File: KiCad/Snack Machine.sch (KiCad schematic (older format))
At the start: 149 parts, among them J1 MDB, J10 Row Screw Terminal, J11 Column Screw Terminal, J12 Display Serial Header, J13 RFID_CONNECTOR, J14 Large Display Header, J2 Power Screw Terminal, J3 RFID Serial Connector, J4 RFID Led Connector, J5 MDB, J6 Door Switch Terminal, J7 LCD EXP1, J8 LCD EXP2, J9 AVR-ISP-6, Q1 P-CH 30V 3.8A, SW1 SW_SPST, U1 MEZD71201A-F, U2 MEZD71202A-G, U3 ATmega2560-16AU, Y1 16MHz

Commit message: Fixing small issue with a missing $EndComp
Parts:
- added D7: D_Schottky, Diodes_SMD:D_SOD-323, symbol Device:D_Schottky
- TP65: Manufacturer Toshiba Semiconductor and Storage -> (none); Part Number CUS10S40,H3F -> (none)
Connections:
- wire segments 386 -> 387
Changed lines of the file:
@@
 	1    4700 1250
 	-1   0    0    1
+$EndComp
 Text Label 13700 7850 2    50   ~ 0
 TX_DISPLAY

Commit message: removed D1 and D3, left Schottky diodes alone
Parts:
- removed D1: D_Zener, Diode_SMD:D_SMB_Handsoldering, symbol Device:D_Zener
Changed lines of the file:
@@
 	4550 1250 4100 1250
-$Comp
-L Device:D_Zener D?
-U 1 1 5BF22396
-P 4700 1250
-AR Path="/5BCD883C/5BF22396" Ref="D?"  Part="1"
-AR Path="/5BF22396" Ref="D1"  Part="1"
-F 0 "D1" H 4700 1034 50  0000 C CNN
-F 1 "D_Zener" H 4700 1125 50  0000 C CNN
-F 2 "Diode_SMD:D_SMB_Handsoldering" H 4700 1250 50  0001 C CNN
-F 3 "~" H 4700 1250 50  0001 C CNN
-F 4 "Micro Commercial" H 4700 1250 50  0001 C CNN "Manufacturer"
-F 5 "3SMBJ5925B-TP" H 4700 1250 50  0001 C CNN "Part Number"
-	1    4700 1250
-	-1   0    0    1
-$EndComp
 $Comp
 L power:+5V #PWR?

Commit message: tweaked ethernet
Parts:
- D7: footprint Diodes_SMD:D_SOD-323 -> Diode_SMD:D_SOD-323
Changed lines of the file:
@@
 F 0 "D7" H 4700 1034 50  0000 C CNN
 F 1 "D_Schottky" H 4700 1125 50  0000 C CNN
-F 2 "Diodes_SMD:D_SOD-323" H 4700 1250 50  0001 C CNN
+F 2 "Diode_SMD:D_SOD-323" H 4700 1250 50  0001 C CNN
 F 3 "~" H 4700 1250 50  0001 C CNN
 F 4 "Toshiba Semiconductor and Storage" H 4700 1250 50  0001 C CNN "Manufacturer"

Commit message: added footprints for Y3 FB1 FB3 FB2 F1
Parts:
- F1: footprint (none) -> Snack Machine:Keystone_3544-2
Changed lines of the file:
@@
 F 0 "F1" V 1853 1250 50  0000 C CNN
 F 1 "1A" V 1944 1250 50  0000 C CNN
-F 2 "" V 1980 1250 50  0001 C CNN
+F 2 "Snack Machine:Keystone_3544-2" V 1980 1250 50  0001 C CNN
 F 3 "~" H 2050 1250 50  0001 C CNN
 F 4 "Keystone Electronics" V 2050 1250 50  0001 C CNN "Manufacturer"

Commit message: updated motor drive circuitry, annotated
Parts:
- removed J6: Door Switch Terminal, TerminalBlock_Phoenix:TerminalBlock_Phoenix_PT-1,5-2-5.0-H_1x02_P5.00mm_Horizontal, symbol Connector:Screw_Terminal_01x02
- added J?: Conn_01x02, Connector_JST:JST_XH_B02B-XH-A_1x02_P2.50mm_Vertical, symbol Connector_Generic:Conn_01x02
- added TP? (x6): TestPoint, TestPoint:TestPoint_THTPad_D1.0mm_Drill0.5mm, symbol Connector:TestPoint
- R17, R18, R5: value 10K -> 1K
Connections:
- wire segments 387 -> 399
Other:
- note removed: "NOTE: MDB opto-isolated"
- note removed: "NOTE: Maybe same as motor driver?"
- note removed: "NOTE: TEST POINTS!"
- note removed: "NOTE: This file is a work-in-progress. There are many notes which will be removed before release."
- note removed: "NOTE: pick resistor vals"
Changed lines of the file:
@@
 P 13850 6850
 F 0 "R17" H 14000 6900 50  0000 C CNN
-F 1 "10K" H 14000 6800 50  0000 C CNN
+F 1 "1K" H 14000 6800 50  0000 C CNN
 F 2 "Resistor_SMD:R_0603_1608Metric_Pad1.05x0.95mm_HandSolder" V 13780 6850 50  0001 C CNN
 F 3 "~" H 13850 6850 50  0001 C CNN
@@
 P 14200 6850
 F 0 "R18" H 14350 6900 50  0000 C CNN
-F 1 "10K" H 14350 6800 50  0000 C CNN
+F 1 "1K" H 14350 6800 50  0000 C CNN
 F 2 "Resistor_SMD:R_0603_1608Metric_Pad1.05x0.95mm_HandSolder" V 14130 6850 50  0001 C CNN
 F 3 "~" H 14200 6850 50  0001 C CNN
@@
 P 4600 7000
 F 0 "R5" V 4500 7000 50  0000 C CNN
-F 1 "10K" V 4400 7000 50  0000 C CNN
+F 1 "1K" V 4400 7000 50  0000 C CNN
 F 2 "Resistor_SMD:R_0603_1608Metric_Pad1.05x0.95mm_HandSolder" V 4530 7000 50  0001 C CNN
 F 3 "~" H 4600 7000 50  0001 C CNN
@@
 	4000 7000 4300 7000
 Connection ~ 4300 7000
-Text Notes 4000 7300 0    50   ~ 0
-NOTE: pick resistor vals
 $Comp
 L Connector:Screw_Terminal_01x02 J2
@@
 Wire Wire Line
 	9100 5500 9500 5500
-Text Notes 6600 8750 0    50   ~ 0
-NOTE: TEST POINTS!
-Text Notes 3750 6200 0    50   ~ 0
-NOTE: Maybe same as motor driver?
 Wire Wire Line
 	4550 1250 4100 1250
@@
 	1    14050 7600
 	1    0    0    -1
-$EndComp
-$Comp
-L Connector:Screw_Terminal_01x02 J6
-U 1 1 5BF43014
-P 3300 5450
-F 0 "J6" H 3300 5700 50  0000 C CNN
-F 1 "Door Switch Terminal" H 3600 5600 50  0000 C CNN
-F 2 "TerminalBlock_Phoenix:TerminalBlock_Phoenix_PT-1,5-2-5.0-H_1x02_P5.00mm_Horizontal" H 3300 5450 50  0001 C CNN
-F 3 "~" H 3300 5450 50  0001 C CNN
-F 4 "277-1667-ND" H 3300 5450 50  0001 C CNN "Part Number"
-	1    3300 5450
-	-1   0    0    -1
 $EndComp
 $Comp
@@
 Wire Wire Line
 	4750 9450 5300 9450
-Text Notes 650  600  0    50   ~ 0
-NOTE: This file is a work-in-progress.  There are many notes which will be removed before release.
 Text Label 6650 7800 0    50   ~ 0
 RESET_DISPLAY
@@
 Wire Wire Line
 	14900 1150 15200 1150
-Text Notes 4200 7600 0    50   ~ 0
-NOTE: MDB opto-isolated
 $Comp
 L Device:D_Schottky D7
@@
 	1    0    0    -1
 $EndComp
+$Comp
+L power:+24V #PWR?
+U 1 1 5C219549
+P 1300 2200
+F 0 "#PWR?" H 1300 2050 50  0001 C CNN
+F 1 "+24V" H 1300 2350 50  0000 C CNN
+F 2 "" H 1300 2200 50  0001 C CNN
+F 3 "" H 1300 2200 50  0001 C CNN
+	1    1300 2200
+	1    0    0    -1
+$EndComp
+$Comp
+L Connector:TestPoint TP?
+U 1 1 5C219FCE
+P 1400 2300
+AR Path="/5BCD883C/5C219FCE" Ref="TP?"  Part="1"
+AR Path="/5C219FCE" Ref="TP?"  Part="1"
+F 0 "TP?" V 1350 2250 50  0000 L CNN
+F 1 "TestPoint" V 1350 2500 50  0000 L CNN
+F 2 "TestPoint:TestPoint_THTPad_D1.0mm_Drill0.5mm" H 1600 2300 50  0001 C CNN
+F 3 "~" H 1600 2300 50  0001 C CNN
+	1    1400 2300
+	0    1    1    0
+$EndComp
+$Comp
+L Connector:TestPoint TP?
+U 1 1 5C21AB48
+P 1400 2400
+AR Path="/5BCD883C/5C21AB48" Ref="TP?"  Part="1"
+AR Path="/5C21AB48" Ref="TP?"  Part="1"
+F 0 "TP?" V 1350 2350 50  0000 L CNN
+F 1 "TestPoint" V 1350 2600 50  0000 L CNN
+F 2 "TestPoint:TestPoint_THTPad_D1.0mm_Drill0.5mm" H 1600 2400 50  0001 C CNN
+F 3 "~" H 1600 2400 50  0001 C CNN
+	1    1400 2400
+	0    1    1    0
+$EndComp
+Wire Wire Line
+	1300 2200 1300 2300
+Wire Wire Line
+	1300 2400 1400 2400
+Wire Wire Line
+	1400 2300 1300 2300
+Connection ~ 1300 2300
+Wire Wire Line
+	1300 2300 1300 2400
+$Comp
+L power:GND #PWR?
+U 1 1 5C27B4BD
+P 1300 2800
+F 0 "#PWR?" H 1300 2550 50  0001 C CNN
+F 1 "GND" H 1300 2650 50  0000 C CNN
+F 2 "" H 1300 2800 50  0001 C CNN
+F 3 "" H 1300 2800 50  0001 C CNN
+	1    1300 2800
+	1    0    0    -1
+$EndComp
+$Comp
+L Connector:TestPoint TP?
+U 1 1 5C27B5F6
+P 1400 2600
+AR Path="/5BCD883C/5C27B5F6" Ref="TP?"  Part="1"
+AR Path="/5C27B5F6" Ref="TP?"  Part="1"
+F 0 "TP?" V 1350 2550 50  0000 L CNN
+F 1 "TestPoint" V 1350 2800 50  0000 L CNN
+F 2 "TestPoint:TestPoint_THTPad_D1.0mm_Drill0.5mm" H 1600 2600 50  0001 C CNN
+F 3 "~" H 1600 2600 50  0001 C CNN
+	1    1400 2600
+	0    1    1    0
+$EndComp
+$Comp
+L Connector:TestPoint TP?
+U 1 1 5C27B912
+P 1400 2700
+AR Path="/5BCD883C/5C27B912" Ref="TP?"  Part="1"
+AR Path="/5C27B912" Ref="TP?"  Part="1"
+F 0 "TP?" V 1350 2650 50  0000 L CNN
+F 1 "TestPoint" V 1350 2900 50  0000 L CNN
+F 2 "TestPoint:TestPoint_THTPad_D1.0mm_Drill0.5mm" H 1600 2700 50  0001 C CNN
+F 3 "~" H 1600 2700 50  0001 C CNN
+	1    1400 2700
+	0    1    1    0
+$EndComp
+Wire Wire Line
+	1300 2800 1300 2700
+Wire Wire Line
+	1300 2600 1400 2600
+Wire Wire Line
+	1400 2700 1300 2700
+Connection ~ 1300 2700
+Wire Wire Line
+	1300 2700 1300 2600
+$Comp
+L Connector:TestPoint TP?
+U 1 1 5C30E40B
+P 6050 1000
+AR Path="/5BCD883C/5C30E40B" Ref="TP?"  Part="1"
+AR Path="/5C30E40B" Ref="TP?"  Part="1"
+F 0 "TP?" V 6000 950 50  0000 L CNN
+F 1 "TestPoint" V 6000 1200 50  0000 L CNN
+F 2 "TestPoint:TestPoint_THTPad_D1.0mm_Drill0.5mm" H 6250 1000 50  0001 C CNN
+F 3 "~" H 6250 1000 50  0001 C CNN
+	1    6050 1000
+	0    1    1    0
+$EndComp
+$Comp
+L Connector:TestPoint TP?
+U 1 1 5C30E595
+P 6050 1100
+AR Path="/5BCD883C/5C30E595" Ref="TP?"  Part="1"
+AR Path="/5C30E595" Ref="TP?"  Part="1"
+F 0 "TP?" V 6000 1050 50  0000 L CNN
+F 1 "TestPoint" V 6000 1300 50  0000 L CNN
+F 2 "TestPoint:TestPoint_THTPad_D1.0mm_Drill0.5mm" H 6250 1100 50  0001 C CNN
+F 3 "~" H 6250 1100 50  0001 C CNN
+	1    6050 1100
+	0    1    1    0
+$EndComp
+$Comp
+L power:+5V #PWR?
+U 1 1 5C30EA88
+P 5950 900
+AR Path="/5BCD883C/5C30EA88" Ref="#PWR?"  Part="1"
+AR Path="/5C30EA88" Ref="#PWR?"  Part="1"
+F 0 "#PWR?" H 5950 750 50  0001 C CNN
+F 1 "+5V" H 5965 1073 50  0000 C CNN
+F 2 "" H 5950 900 50  0001 C CNN
+F 3 "" H 5950 900 50  0001 C CNN
+	1    5950 900
+	1    0    0    -1
+$EndComp
+Wire Wire Line
+	5950 900  5950 1000
+Wire Wire Line
+	5950 1100 6050 1100
+Wire Wire Line
+	6050 1000 5950 1000
+Connection ~ 5950 1000
+Wire Wire Line
+	5950 1000 5950 1100
+$Comp
+L Connector_Generic:Conn_01x02 J?
+U 1 1 5C7C3A6B
+P 3300 5450
+F 0 "J?" H 3350 5700 50  0000 C CNN
+F 1 "Conn_01x02" H 3350 5600 50  0000 C CNN
+F 2 "Connector_JST:JST_XH_B02B-XH-A_1x02_P2.50mm_Vertical" H 3300 5450 50  0001 C CNN
+F 3 "~" H 3300 5450 50  0001 C CNN
+	1    3300 5450
+	-1   0    0    -1
+$EndComp
 $EndSCHEMATC

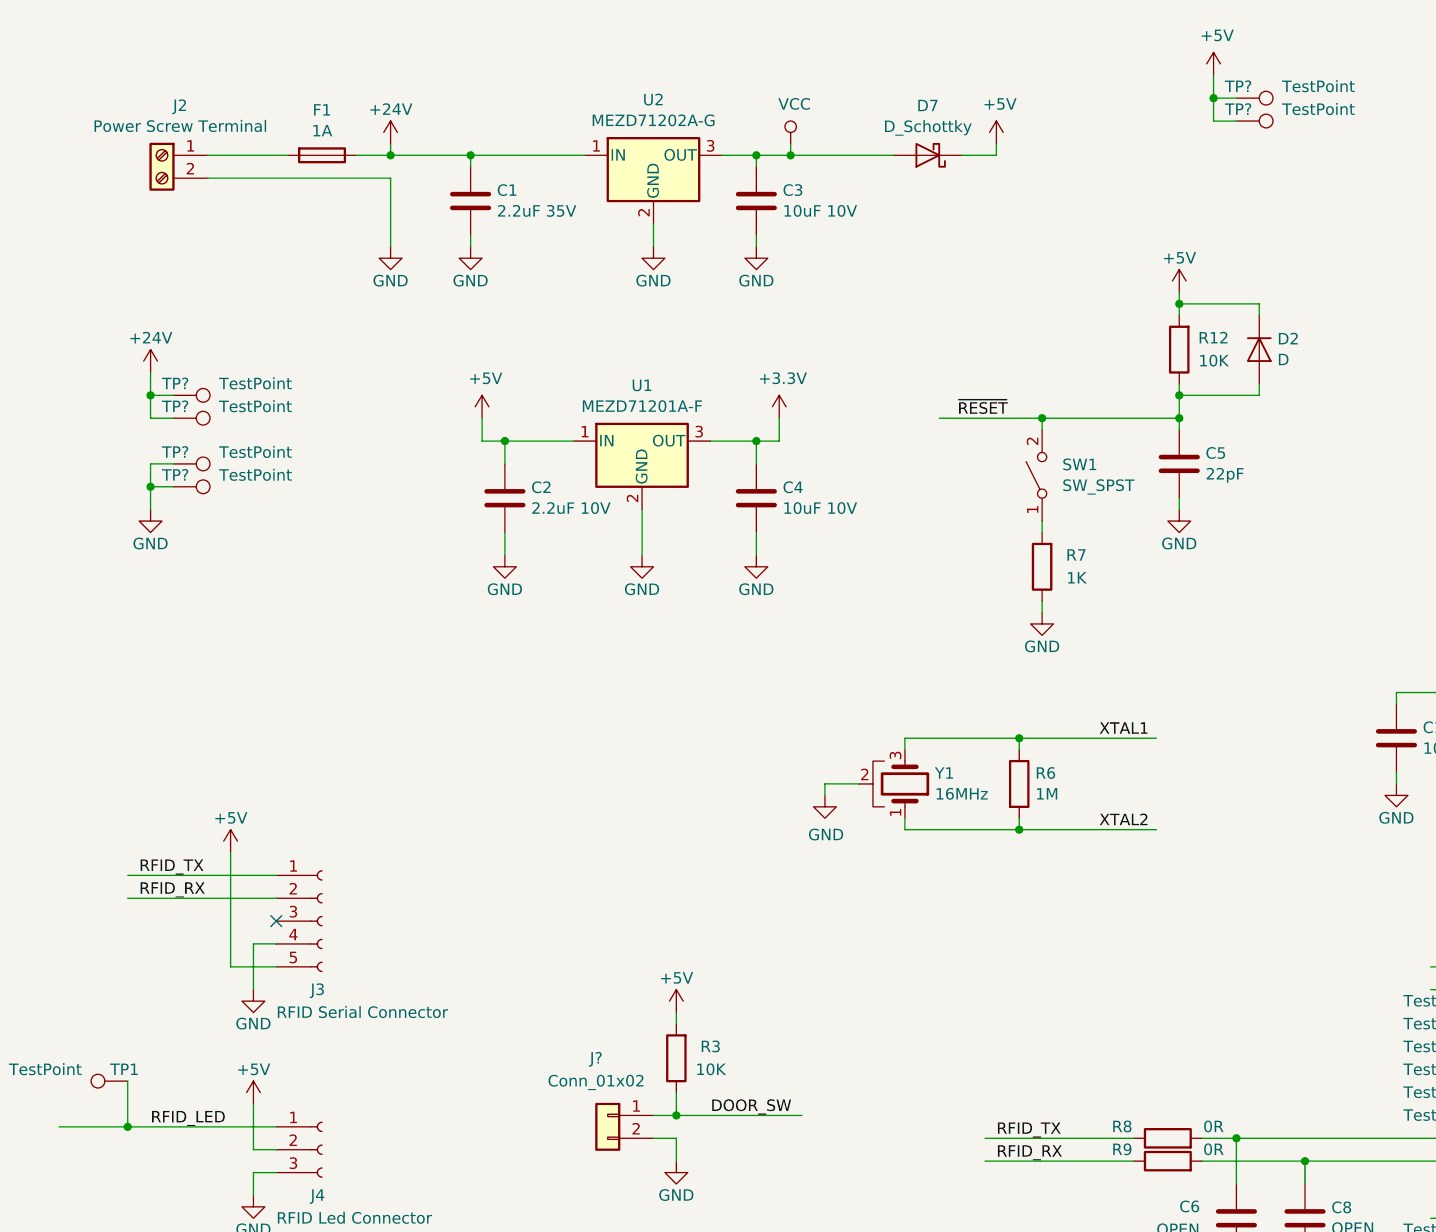
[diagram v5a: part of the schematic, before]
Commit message: fixed S2A and motor drive capacitor footprint links
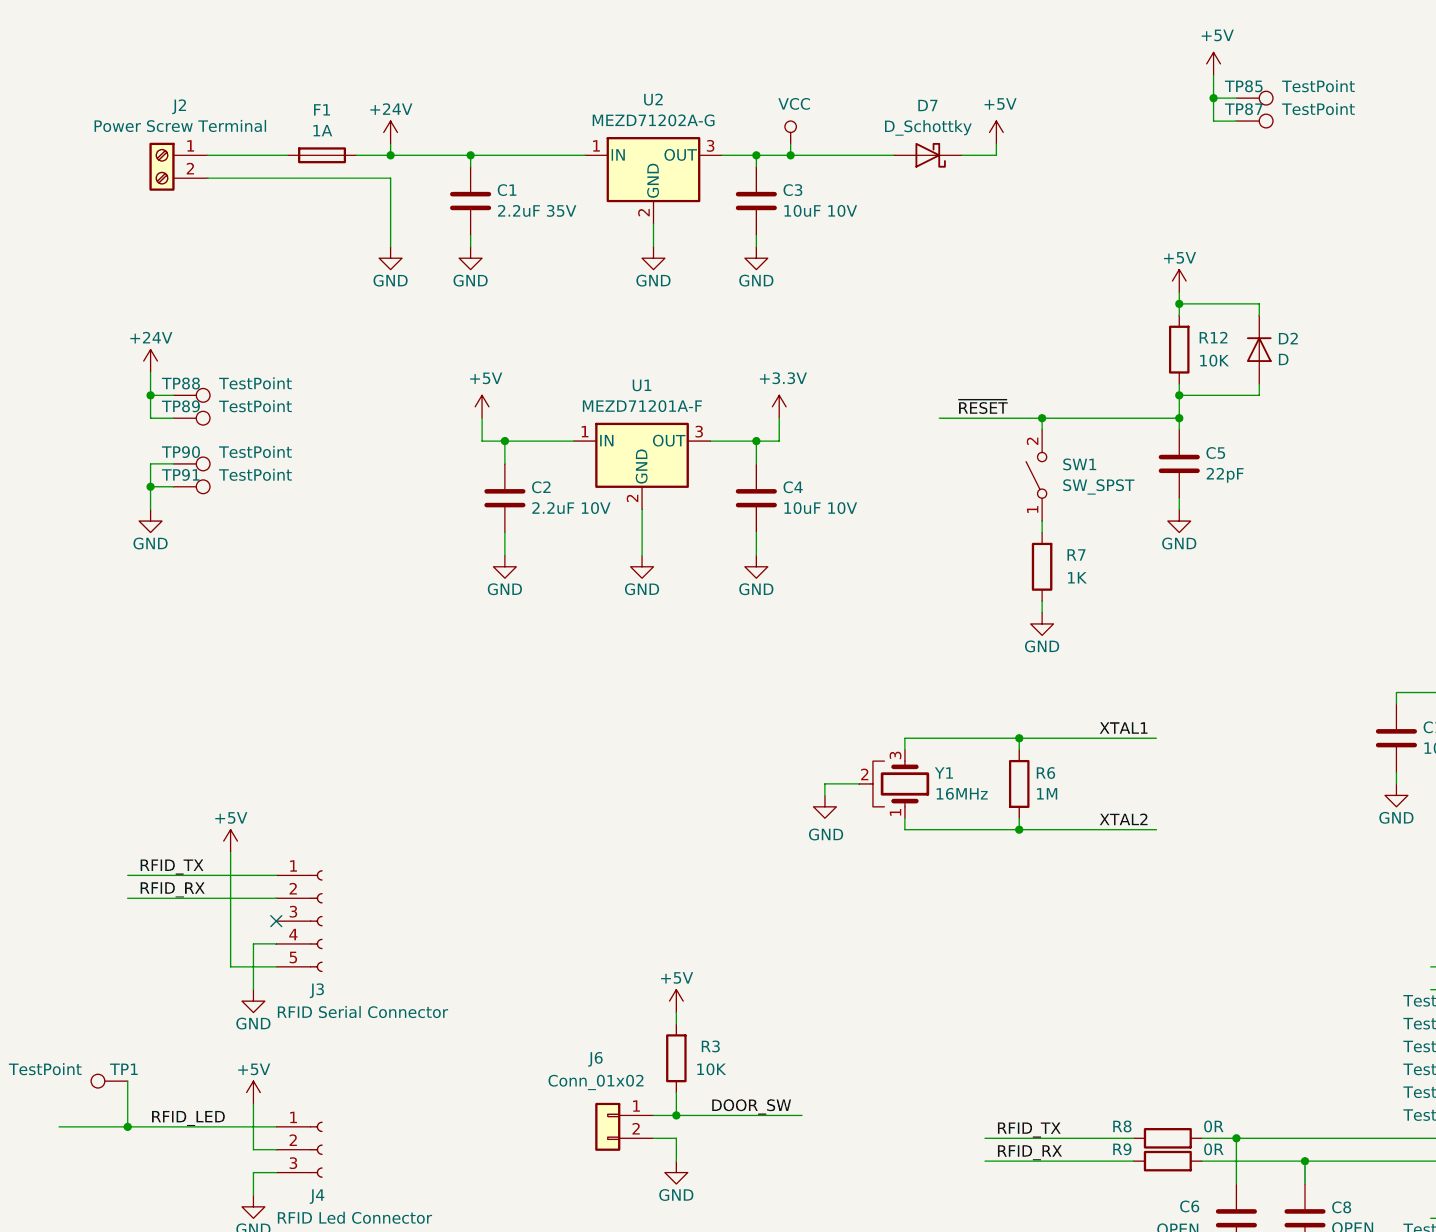
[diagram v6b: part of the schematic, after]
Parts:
- gave numbers to parts that had none: 7
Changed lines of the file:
@@
 $EndComp
 $Comp
-L power:+24V #PWR?
+L power:+24V #PWR070
 U 1 1 5C219549
 P 1300 2200
-F 0 "#PWR?" H 1300 2050 50  0001 C CNN
+F 0 "#PWR070" H 1300 2050 50  0001 C CNN
 F 1 "+24V" H 1300 2350 50  0000 C CNN
 F 2 "" H 1300 2200 50  0001 C CNN
@@
 P 1400 2300
 AR Path="/5BCD883C/5C219FCE" Ref="TP?"  Part="1"
-AR Path="/5C219FCE" Ref="TP?"  Part="1"
-F 0 "TP?" V 1350 2250 50  0000 L CNN
+AR Path="/5C219FCE" Ref="TP88"  Part="1"
+F 0 "TP88" V 1350 2250 50  0000 L CNN
 F 1 "TestPoint" V 1350 2500 50  0000 L CNN
 F 2 "TestPoint:TestPoint_THTPad_D1.0mm_Drill0.5mm" H 1600 2300 50  0001 C CNN
@@
 P 1400 2400
 AR Path="/5BCD883C/5C21AB48" Ref="TP?"  Part="1"
-AR Path="/5C21AB48" Ref="TP?"  Part="1"
-F 0 "TP?" V 1350 2350 50  0000 L CNN
+AR Path="/5C21AB48" Ref="TP89"  Part="1"
+F 0 "TP89" V 1350 2350 50  0000 L CNN
 F 1 "TestPoint" V 1350 2600 50  0000 L CNN
 F 2 "TestPoint:TestPoint_THTPad_D1.0mm_Drill0.5mm" H 1600 2400 50  0001 C CNN
@@
 	1300 2300 1300 2400
 $Comp
-L power:GND #PWR?
+L power:GND #PWR076
 U 1 1 5C27B4BD
 P 1300 2800
-F 0 "#PWR?" H 1300 2550 50  0001 C CNN
+F 0 "#PWR076" H 1300 2550 50  0001 C CNN
 F 1 "GND" H 1300 2650 50  0000 C CNN
 F 2 "" H 1300 2800 50  0001 C CNN
@@
 P 1400 2600
 AR Path="/5BCD883C/5C27B5F6" Ref="TP?"  Part="1"
-AR Path="/5C27B5F6" Ref="TP?"  Part="1"
-F 0 "TP?" V 1350 2550 50  0000 L CNN
+AR Path="/5C27B5F6" Ref="TP90"  Part="1"
+F 0 "TP90" V 1350 2550 50  0000 L CNN
 F 1 "TestPoint" V 1350 2800 50  0000 L CNN
 F 2 "TestPoint:TestPoint_THTPad_D1.0mm_Drill0.5mm" H 1600 2600 50  0001 C CNN
@@
 P 1400 2700
 AR Path="/5BCD883C/5C27B912" Ref="TP?"  Part="1"
-AR Path="/5C27B912" Ref="TP?"  Part="1"
-F 0 "TP?" V 1350 2650 50  0000 L CNN
+AR Path="/5C27B912" Ref="TP91"  Part="1"
+F 0 "TP91" V 1350 2650 50  0000 L CNN
 F 1 "TestPoint" V 1350 2900 50  0000 L CNN
 F 2 "TestPoint:TestPoint_THTPad_D1.0mm_Drill0.5mm" H 1600 2700 50  0001 C CNN
@@
 P 6050 1000
 AR Path="/5BCD883C/5C30E40B" Ref="TP?"  Part="1"
-AR Path="/5C30E40B" Ref="TP?"  Part="1"
-F 0 "TP?" V 6000 950 50  0000 L CNN
+AR Path="/5C30E40B" Ref="TP85"  Part="1"
+F 0 "TP85" V 6000 950 50  0000 L CNN
 F 1 "TestPoint" V 6000 1200 50  0000 L CNN
 F 2 "TestPoint:TestPoint_THTPad_D1.0mm_Drill0.5mm" H 6250 1000 50  0001 C CNN
@@
 P 6050 1100
 AR Path="/5BCD883C/5C30E595" Ref="TP?"  Part="1"
-AR Path="/5C30E595" Ref="TP?"  Part="1"
-F 0 "TP?" V 6000 1050 50  0000 L CNN
+AR Path="/5C30E595" Ref="TP87"  Part="1"
+F 0 "TP87" V 6000 1050 50  0000 L CNN
 F 1 "TestPoint" V 6000 1300 50  0000 L CNN
 F 2 "TestPoint:TestPoint_THTPad_D1.0mm_Drill0.5mm" H 6250 1100 50  0001 C CNN
@@
 P 5950 900
 AR Path="/5BCD883C/5C30EA88" Ref="#PWR?"  Part="1"
-AR Path="/5C30EA88" Ref="#PWR?"  Part="1"
-F 0 "#PWR?" H 5950 750 50  0001 C CNN
+AR Path="/5C30EA88" Ref="#PWR068"  Part="1"
+F 0 "#PWR068" H 5950 750 50  0001 C CNN
 F 1 "+5V" H 5965 1073 50  0000 C CNN
 F 2 "" H 5950 900 50  0001 C CNN
@@
 	5950 1000 5950 1100
 $Comp
-L Connector_Generic:Conn_01x02 J?
+L Connector_Generic:Conn_01x02 J6
 U 1 1 5C7C3A6B
 P 3300 5450
-F 0 "J?" H 3350 5700 50  0000 C CNN
+F 0 "J6" H 3350 5700 50  0000 C CNN
 F 1 "Conn_01x02" H 3350 5600 50  0000 C CNN
 F 2 "Connector_JST:JST_XH_B02B-XH-A_1x02_P2.50mm_Vertical" H 3300 5450 50  0001 C CNN

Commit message: Updated Schematic
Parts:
- Q1: footprint Package_TO_SOT_SMD:SOT-23_Handsoldering -> Snack Machine:SOT-23_Handsoldering_Lite
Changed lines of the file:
@@
 F 0 "Q1" V 4343 6600 50  0000 C CNN
 F 1 "P-CH 30V 3.8A" V 4252 6600 50  0000 C CNN
-F 2 "Package_TO_SOT_SMD:SOT-23_Handsoldering" H 4200 6525 50  0001 L CIN
+F 2 "Snack Machine:SOT-23_Handsoldering_Lite" H 4200 6525 50  0001 L CIN
 F 3 "~" H 4000 6600 50  0001 L CNN
 F 4 "Diodes Incorporated" H 4000 6600 50  0001 C CNN "Manufacturer"

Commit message: rearranging footprints on layout
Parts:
- TP1, TP10, TP11, TP12, TP13, TP14, TP15, TP16, TP17, TP18, TP19, TP2, TP20, TP21, TP22, TP23, TP24, TP25, TP26, TP27, TP28, TP29, TP3, TP30, TP31, TP32, TP33, TP34, TP35, TP36, TP37, TP38, TP39, TP4, TP40, TP41, TP42, TP43, TP44, TP45, TP46, TP47, TP48, TP49, TP5, TP50, TP51, TP52, TP53, TP54, TP55, TP56, TP57, TP58, TP59, TP6, TP60, TP61, TP62, TP63, TP64, TP65, TP66, TP67, TP68, TP69, TP7, TP70, TP71, TP72, TP73, TP74, TP75, TP76, TP77, TP78, TP79, TP8, TP80, TP81, TP82, TP83, TP84, TP85, TP87, TP88, TP89, TP9, TP90, TP91: footprint TestPoint:TestPoint_THTPad_D1.0mm_Drill0.5mm -> Snack Machine:TestPoint_THTPad_D0.8mm_Drill0.4mm
